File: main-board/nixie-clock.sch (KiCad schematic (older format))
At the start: 9 parts

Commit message: Rozdzielenie projektu
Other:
- note added: "Zamienić na EXTI?"
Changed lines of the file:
@@
 Text Label 9500 3850 2    60   ~ 0
 BRIGHT_POT
+Text Notes 9600 3850 0    60   ~ 0
+Zamienić na EXTI?
 $EndSCHEMATC

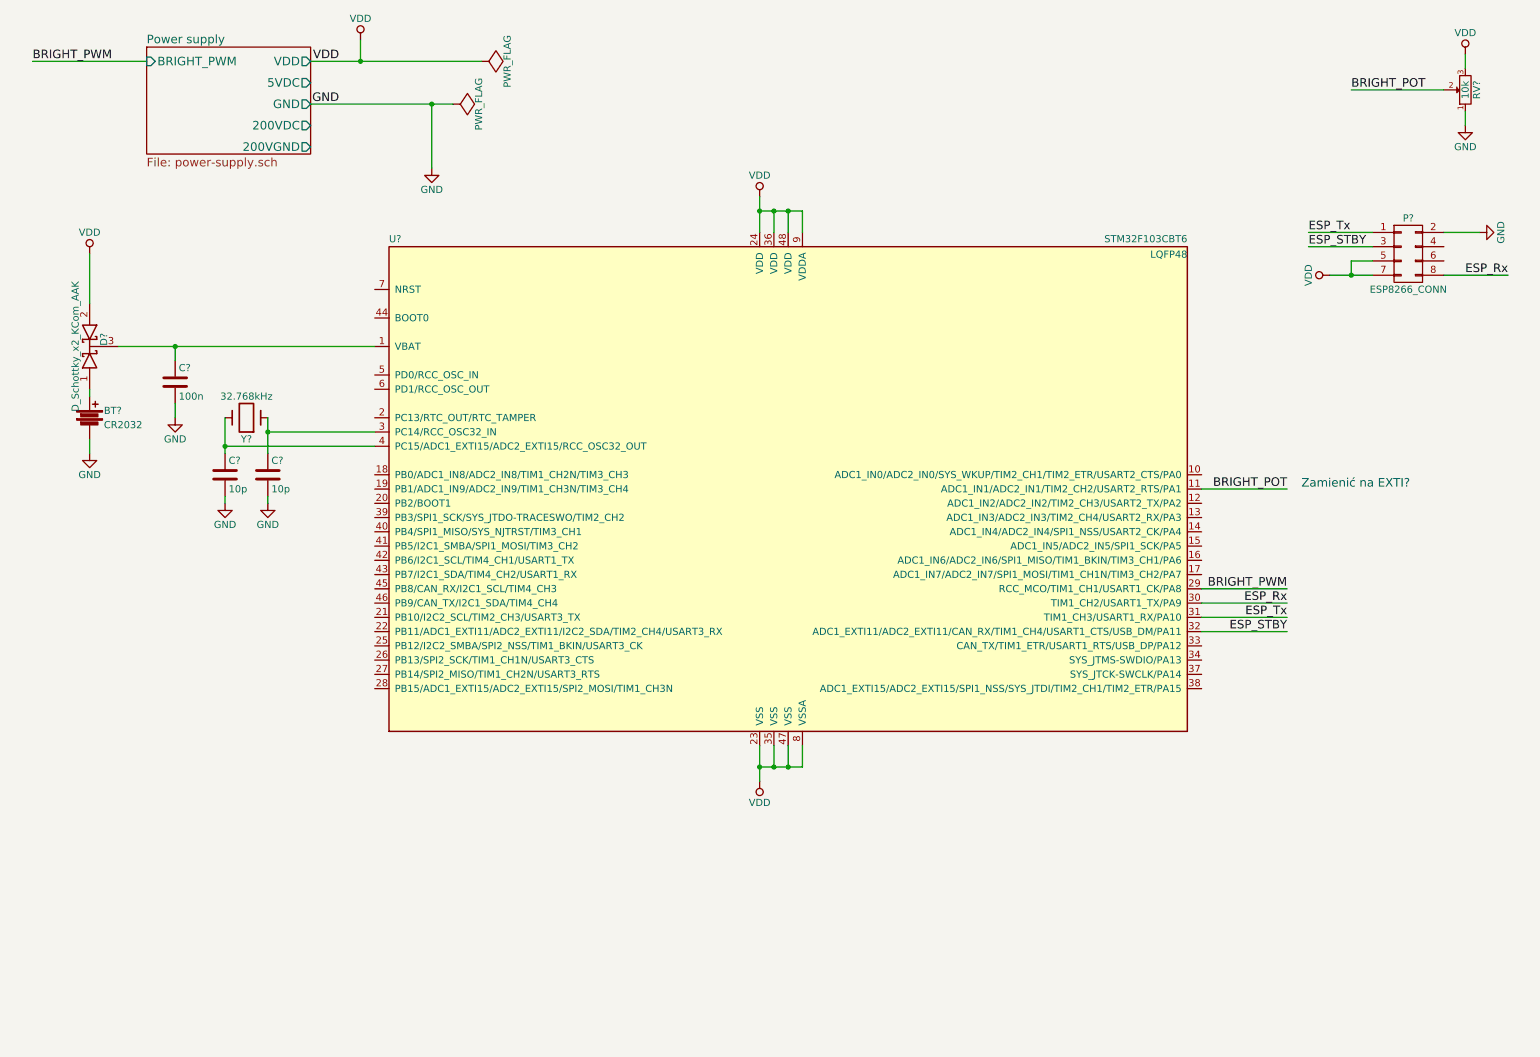
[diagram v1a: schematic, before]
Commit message: GPIO Expander - podlaczenie do STM32; wyprowadzenia dla modulow NIXIE; zasilanie - do poprawki (GPIO Expander zasilany z 5V - STM 3,3V
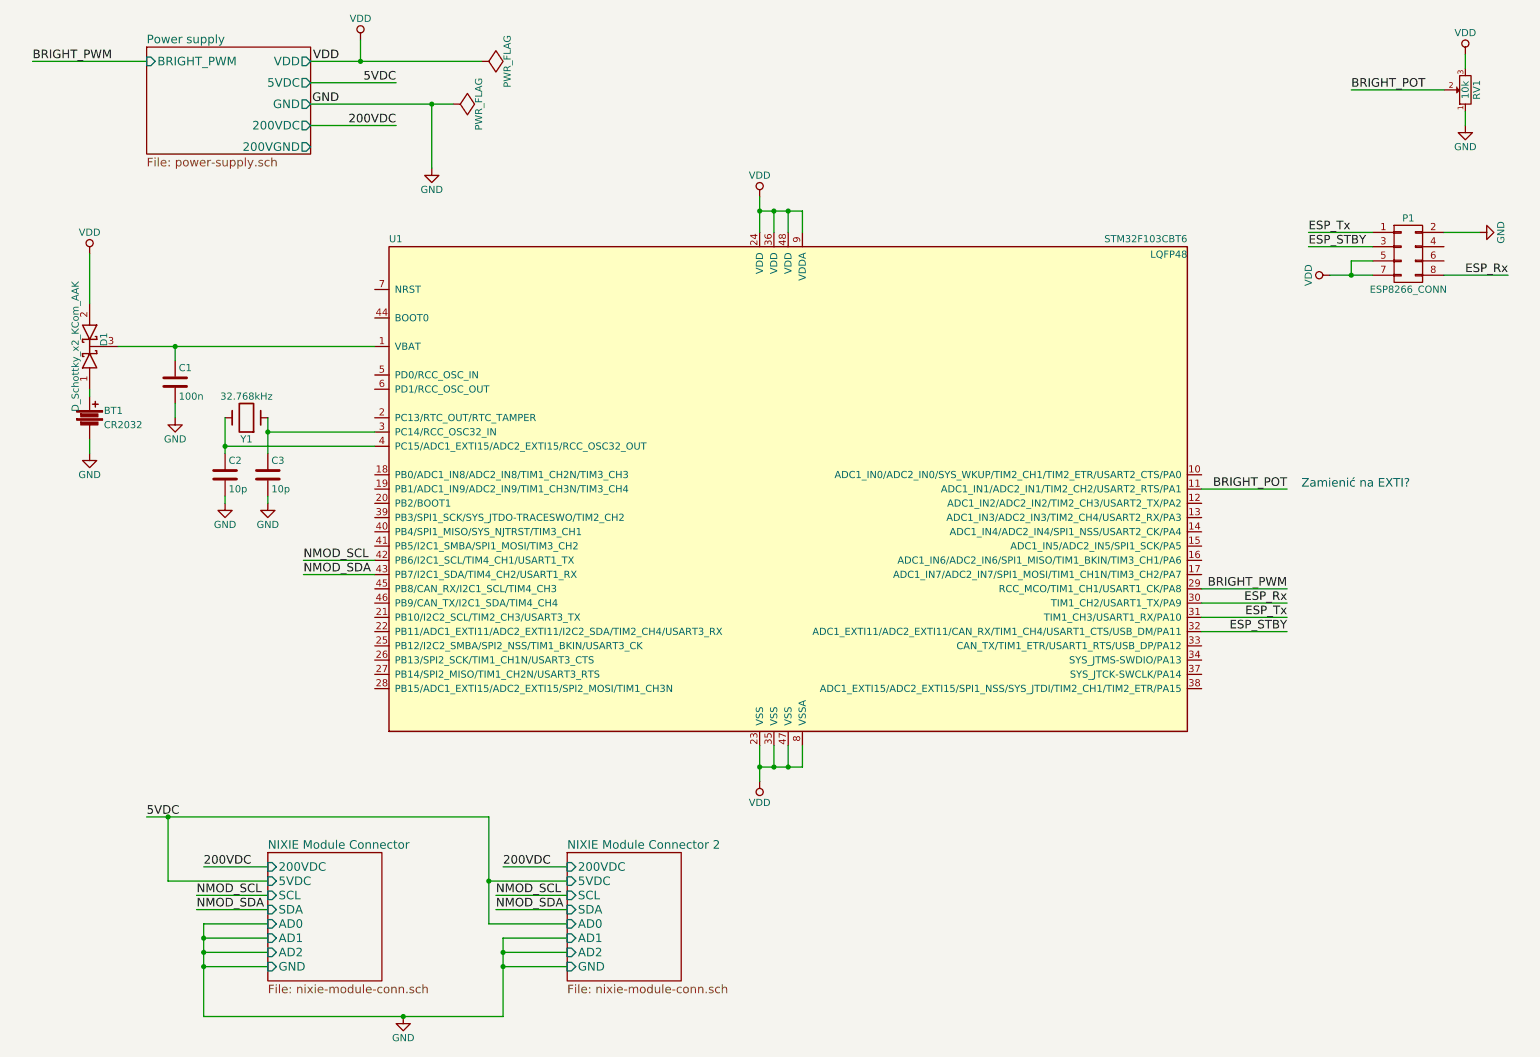
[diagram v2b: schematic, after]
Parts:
- gave numbers to parts that had none: 9
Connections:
- net NMOD_SCL: now reaches U1.42 (PB6/I2C1_SCL/TIM4_CH1/USART1_TX)
- net NMOD_SDA: now reaches U1.43 (PB7/I2C1_SDA/TIM4_CH2/USART1_RX)
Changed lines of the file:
@@
 $Descr A4 11693 8268
 encoding utf-8
-Sheet 1 2
+Sheet 1 4
 Title ""
 Date ""
@@
 $EndDescr
 $Comp
-L STM32F103CBTx U?
+L STM32F103CBTx U1
 U 1 1 5809D886
 P 6000 3850
-F 0 "U?" H 3200 5575 50  0000 L BNN
+F 0 "U1" H 3200 5575 50  0000 L BNN
 F 1 "STM32F103CBT6" H 8800 5575 50  0000 R BNN
 F 2 "LQFP48" H 8800 5525 50  0000 R TNN
@@
 $EndComp
 $Comp
-L Crystal Y?
+L Crystal Y1
 U 1 1 5809F07A
 P 2200 3350
-F 0 "Y?" H 2200 3500 50  0000 C CNN
+F 0 "Y1" H 2200 3500 50  0000 C CNN
 F 1 "32.768kHz" H 2200 3200 50  0000 C CNN
 F 2 "" H 2200 3350 50  0000 C CNN
@@
 	2050 3550 3100 3550
 $Comp
-L C C?
+L C C2
 U 1 1 5809F25A
 P 2050 3750
-F 0 "C?" H 2075 3850 50  0000 L CNN
+F 0 "C2" H 2075 3850 50  0000 L CNN
 F 1 "10p" H 2075 3650 50  0000 L CNN
 F 2 "" H 2088 3600 50  0000 C CNN
@@
 $EndComp
 $Comp
-L C C?
+L C C3
 U 1 1 5809F3ED
 P 2350 3750
-F 0 "C?" H 2375 3850 50  0000 L CNN
+F 0 "C3" H 2375 3850 50  0000 L CNN
 F 1 "10p" H 2375 3650 50  0000 L CNN
 F 2 "" H 2388 3600 50  0000 C CNN
@@
 $EndComp
 $Comp
-L GND #PWR?
+L GND #PWR01
 U 1 1 5809F415
 P 2050 3950
-F 0 "#PWR?" H 2050 3700 50  0001 C CNN
+F 0 "#PWR01" H 2050 3700 50  0001 C CNN
 F 1 "GND" H 2050 3800 50  0000 C CNN
 F 2 "" H 2050 3950 50  0000 C CNN
@@
 $EndComp
 $Comp
-L GND #PWR?
+L GND #PWR02
 U 1 1 5809F43C
 P 2350 3950
-F 0 "#PWR?" H 2350 3700 50  0001 C CNN
+F 0 "#PWR02" H 2350 3700 50  0001 C CNN
 F 1 "GND" H 2350 3800 50  0000 C CNN
 F 2 "" H 2350 3950 50  0000 C CNN
@@
 	2350 3900 2350 3950
 $Comp
-L D_Schottky_x2_KCom_AAK D?
+L D_Schottky_x2_KCom_AAK D1
 U 1 1 580A07B6
 P 1100 2850
-F 0 "D?" H 1150 2750 50  0000 C CNN
+F 0 "D1" H 1150 2750 50  0000 C CNN
 F 1 "D_Schottky_x2_KCom_AAK" H 1100 2950 50  0000 C CNN
 F 2 "" H 1100 2850 50  0000 C CNN
@@
 Connection ~ 1700 2850
 $Comp
-L C C?
+L C C1
 U 1 1 580A0B7E
 P 1700 3100
-F 0 "C?" H 1725 3200 50  0000 L CNN
+F 0 "C1" H 1725 3200 50  0000 L CNN
 F 1 "100n" H 1725 3000 50  0000 L CNN
 F 2 "" H 1738 2950 50  0000 C CNN
@@
 $EndComp
 $Comp
-L GND #PWR?
+L GND #PWR03
 U 1 1 580A0C6B
 P 1700 3350
-F 0 "#PWR?" H 1700 3100 50  0001 C CNN
+F 0 "#PWR03" H 1700 3100 50  0001 C CNN
 F 1 "GND" H 1700 3200 50  0000 C CNN
 F 2 "" H 1700 3350 50  0000 C CNN
@@
 	1700 3350 1700 3250
 $Comp
-L Battery BT?
+L Battery BT1
 U 1 1 580A0D26
 P 1100 3350
-F 0 "BT?" H 1200 3400 50  0000 L CNN
+F 0 "BT1" H 1200 3400 50  0000 L CNN
 F 1 "CR2032" H 1200 3300 50  0000 L CNN
 F 2 "" V 1100 3390 50  0000 C CNN
@@
 	1100 3200 1100 3150
 $Comp
-L GND #PWR?
+L GND #PWR04
 U 1 1 580A0DB8
 P 1100 3600
-F 0 "#PWR?" H 1100 3350 50  0001 C CNN
+F 0 "#PWR04" H 1100 3350 50  0001 C CNN
 F 1 "GND" H 1100 3450 50  0000 C CNN
 F 2 "" H 1100 3600 50  0000 C CNN
@@
 $EndSheet
 $Comp
-L PWR_FLAG #FLG?
+L PWR_FLAG #FLG05
 U 1 1 581749DC
 P 3850 850
-F 0 "#FLG?" H 3850 945 50  0001 C CNN
+F 0 "#FLG05" H 3850 945 50  0001 C CNN
 F 1 "PWR_FLAG" H 3850 1030 50  0000 C CNN
 F 2 "" H 3850 850 50  0000 C CNN
@@
 $EndComp
 $Comp
-L PWR_FLAG #FLG?
+L PWR_FLAG #FLG06
 U 1 1 58174A1B
 P 3650 1150
-F 0 "#FLG?" H 3650 1245 50  0001 C CNN
+F 0 "#FLG06" H 3650 1245 50  0001 C CNN
 F 1 "PWR_FLAG" H 3650 1330 50  0000 C CNN
 F 2 "" H 3650 1150 50  0000 C CNN
@@
 Connection ~ 6000 5800
 $Comp
-L GND #PWR?
+L GND #PWR07
 U 1 1 58173306
 P 3500 1600
-F 0 "#PWR?" H 3500 1350 50  0001 C CNN
+F 0 "#PWR07" H 3500 1350 50  0001 C CNN
 F 1 "GND" H 3500 1450 50  0000 C CNN
 F 2 "" H 3500 1600 50  0000 C CNN
@@
 Connection ~ 3500 1150
 $Comp
-L VDD #PWR?
+L VDD #PWR08
 U 1 1 58175A0D
 P 3000 700
-F 0 "#PWR?" H 3000 550 50  0001 C CNN
+F 0 "#PWR08" H 3000 550 50  0001 C CNN
 F 1 "VDD" H 3000 850 50  0000 C CNN
 F 2 "" H 3000 700 50  0000 C CNN
@@
 $EndComp
 $Comp
-L VDD #PWR?
+L VDD #PWR09
 U 1 1 58176266
 P 1100 2200
-F 0 "#PWR?" H 1100 2050 50  0001 C CNN
+F 0 "#PWR09" H 1100 2050 50  0001 C CNN
 F 1 "VDD" H 1100 2350 50  0000 C CNN
 F 2 "" H 1100 2200 50  0000 C CNN
@@
 $EndComp
 $Comp
-L VDD #PWR?
+L VDD #PWR010
 U 1 1 58176451
 P 5800 1800
-F 0 "#PWR?" H 5800 1650 50  0001 C CNN
+F 0 "#PWR010" H 5800 1650 50  0001 C CNN
 F 1 "VDD" H 5800 1950 50  0000 C CNN
 F 2 "" H 5800 1800 50  0000 C CNN
@@
 $EndComp
 $Comp
-L VDD #PWR?
+L VDD #PWR011
 U 1 1 58176B17
 P 5800 5900
-F 0 "#PWR?" H 5800 5750 50  0001 C CNN
+F 0 "#PWR011" H 5800 5750 50  0001 C CNN
 F 1 "VDD" H 5800 6050 50  0000 C CNN
 F 2 "" H 5800 5900 50  0000 C CNN
@@
 Connection ~ 3000 850
 $Comp
-L CONN_02X04 P?
+L CONN_02X04 P1
 U 1 1 5817ACF2
 P 10350 2200
-F 0 "P?" H 10350 2450 50  0000 C CNN
+F 0 "P1" H 10350 2450 50  0000 C CNN
 F 1 "ESP8266_CONN" H 10350 1950 50  0000 C CNN
 F 2 "" H 10350 1000 50  0000 C CNN
@@
 	10600 2050 10850 2050
 $Comp
-L GND #PWR?
+L GND #PWR012
 U 1 1 5817B257
 P 10850 2050
-F 0 "#PWR?" H 10850 1800 50  0001 C CNN
+F 0 "#PWR012" H 10850 1800 50  0001 C CNN
 F 1 "GND" H 10850 1900 50  0000 C CNN
 F 2 "" H 10850 2050 50  0000 C CNN
@@
 $EndComp
 $Comp
-L VDD #PWR?
+L VDD #PWR013
 U 1 1 5817B5C8
 P 9800 2350
-F 0 "#PWR?" H 9800 2200 50  0001 C CNN
+F 0 "#PWR013" H 9800 2200 50  0001 C CNN
 F 1 "VDD" H 9800 2500 50  0000 C CNN
 F 2 "" H 9800 2350 50  0000 C CNN
@@
 BRIGHT_PWM
 $Comp
-L POT RV?
+L POT RV1
 U 1 1 58181F47
 P 10750 1050
-F 0 "RV?" H 10750 970 50  0000 C CNN
+F 0 "RV1" H 10750 970 50  0000 C CNN
 F 1 "10k" H 10750 1050 50  0000 C CNN
 F 2 "" H 10750 1050 50  0000 C CNN
@@
 	10750 1200 10750 1300
 $Comp
-L VDD #PWR?
+L VDD #PWR014
 U 1 1 58182C82
 P 10750 800
-F 0 "#PWR?" H 10750 650 50  0001 C CNN
+F 0 "#PWR014" H 10750 650 50  0001 C CNN
 F 1 "VDD" H 10750 950 50  0000 C CNN
 F 2 "" H 10750 800 50  0000 C CNN
@@
 $EndComp
 $Comp
-L GND #PWR?
+L GND #PWR015
 U 1 1 58182F5B
 P 10750 1300
-F 0 "#PWR?" H 10750 1050 50  0001 C CNN
+F 0 "#PWR015" H 10750 1050 50  0001 C CNN
 F 1 "GND" H 10750 1150 50  0000 C CNN
 F 2 "" H 10750 1300 50  0000 C CNN
@@
 Text Notes 9600 3850 0    60   ~ 0
 Zamienić na EXTI?
+$Sheet
+S 2350 6400 800  900
+U 58191DB1
+F0 "NIXIE Module Connector" 60
+F1 "nixie-module-conn.sch" 60
+F2 "SCL" I L 2350 6700 60
+F3 "SDA" I L 2350 6800 60
+F4 "AD0" I L 2350 6900 60
+F5 "AD1" I L 2350 7000 60
+F6 "AD2" I L 2350 7100 60
+F7 "5VDC" I L 2350 6600 60
+F8 "GND" I L 2350 7200 60
+F9 "200VDC" I L 2350 6500 60
+$EndSheet
+$Sheet
+S 4450 6400 800  900
+U 581979CF
+F0 "NIXIE Module Connector 2" 60
+F1 "nixie-module-conn.sch" 60
+F2 "SCL" I L 4450 6700 60
+F3 "SDA" I L 4450 6800 60
+F4 "AD0" I L 4450 6900 60
+F5 "AD1" I L 4450 7000 60
+F6 "AD2" I L 4450 7100 60
+F7 "5VDC" I L 4450 6600 60
+F8 "GND" I L 4450 7200 60
+F9 "200VDC" I L 4450 6500 60
+$EndSheet
+Wire Wire Line
+	2650 1300 3250 1300
+Wire Wire Line
+	2650 1000 3250 1000
+Text Label 3250 1000 2    60   ~ 0
+5VDC
+Text Label 3250 1300 2    60   ~ 0
+200VDC
+Wire Wire Line
+	2350 6500 1900 6500
+Text Label 1900 6500 0    60   ~ 0
+200VDC
+Wire Wire Line
+	1650 6600 2350 6600
+Text Label 4000 6500 0    60   ~ 0
+200VDC
+Text Label 1500 6150 0    60   ~ 0
+5VDC
+Wire Wire Line
+	4000 6500 4450 6500
+Wire Wire Line
+	3900 6600 4450 6600
+$Comp
+L GND #PWR?
+U 1 1 5819F48F
+P 3300 7550
+F 0 "#PWR?" H 3300 7300 50  0001 C CNN
+F 1 "GND" H 3300 7400 50  0000 C CNN
+F 2 "" H 3300 7550 50  0000 C CNN
+F 3 "" H 3300 7550 50  0000 C CNN
+	1    3300 7550
+	1    0    0    -1
+$EndComp
+Wire Wire Line
+	4450 7200 4000 7200
+Wire Wire Line
+	4000 7000 4000 7550
+Wire Wire Line
+	4000 7550 1900 7550
+Wire Wire Line
+	1900 7550 1900 6900
+Wire Wire Line
+	1900 7200 2350 7200
+Connection ~ 3300 7550
+Wire Wire Line
+	1650 6150 1650 6600
+Wire Wire Line
+	1500 6150 3900 6150
+Wire Wire Line
+	3900 6150 3900 6900
+Connection ~ 1650 6150
+Wire Wire Line
+	1900 6900 2350 6900
+Connection ~ 1900 7200
+Wire Wire Line
+	2350 7000 1900 7000
+Connection ~ 1900 7000
+Wire Wire Line
+	2350 7100 1900 7100
+Connection ~ 1900 7100
+Wire Wire Line
+	3900 6900 4450 6900
+Connection ~ 3900 6600
+Wire Wire Line
+	4450 7000 4000 7000
+Connection ~ 4000 7200
+Wire Wire Line
+	4450 7100 4000 7100
+Connection ~ 4000 7100
+Wire Wire Line
+	2600 4350 3100 4350
+Wire Wire Line
+	2600 4450 3100 4450
+Text Label 2600 4350 0    60   ~ 0
+NMOD_SCL
+Text Label 2600 4450 0    60   ~ 0
+NMOD_SDA
+Wire Wire Line
+	1850 6700 2350 6700
+Wire Wire Line
+	1850 6800 2350 6800
+Wire Wire Line
+	3950 6700 4450 6700
+Wire Wire Line
+	3950 6800 4450 6800
+Text Label 3950 6700 0    60   ~ 0
+NMOD_SCL
+Text Label 3950 6800 0    60   ~ 0
+NMOD_SDA
+Text Label 1850 6700 0    60   ~ 0
+NMOD_SCL
+Text Label 1850 6800 0    60   ~ 0
+NMOD_SDA
 $EndSCHEMATC

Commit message: Dokumentacja STM32F103CBT6; poprawki zasilania, podciagniecie linii SDA i SCL, kondensator przy ESP8266 #1
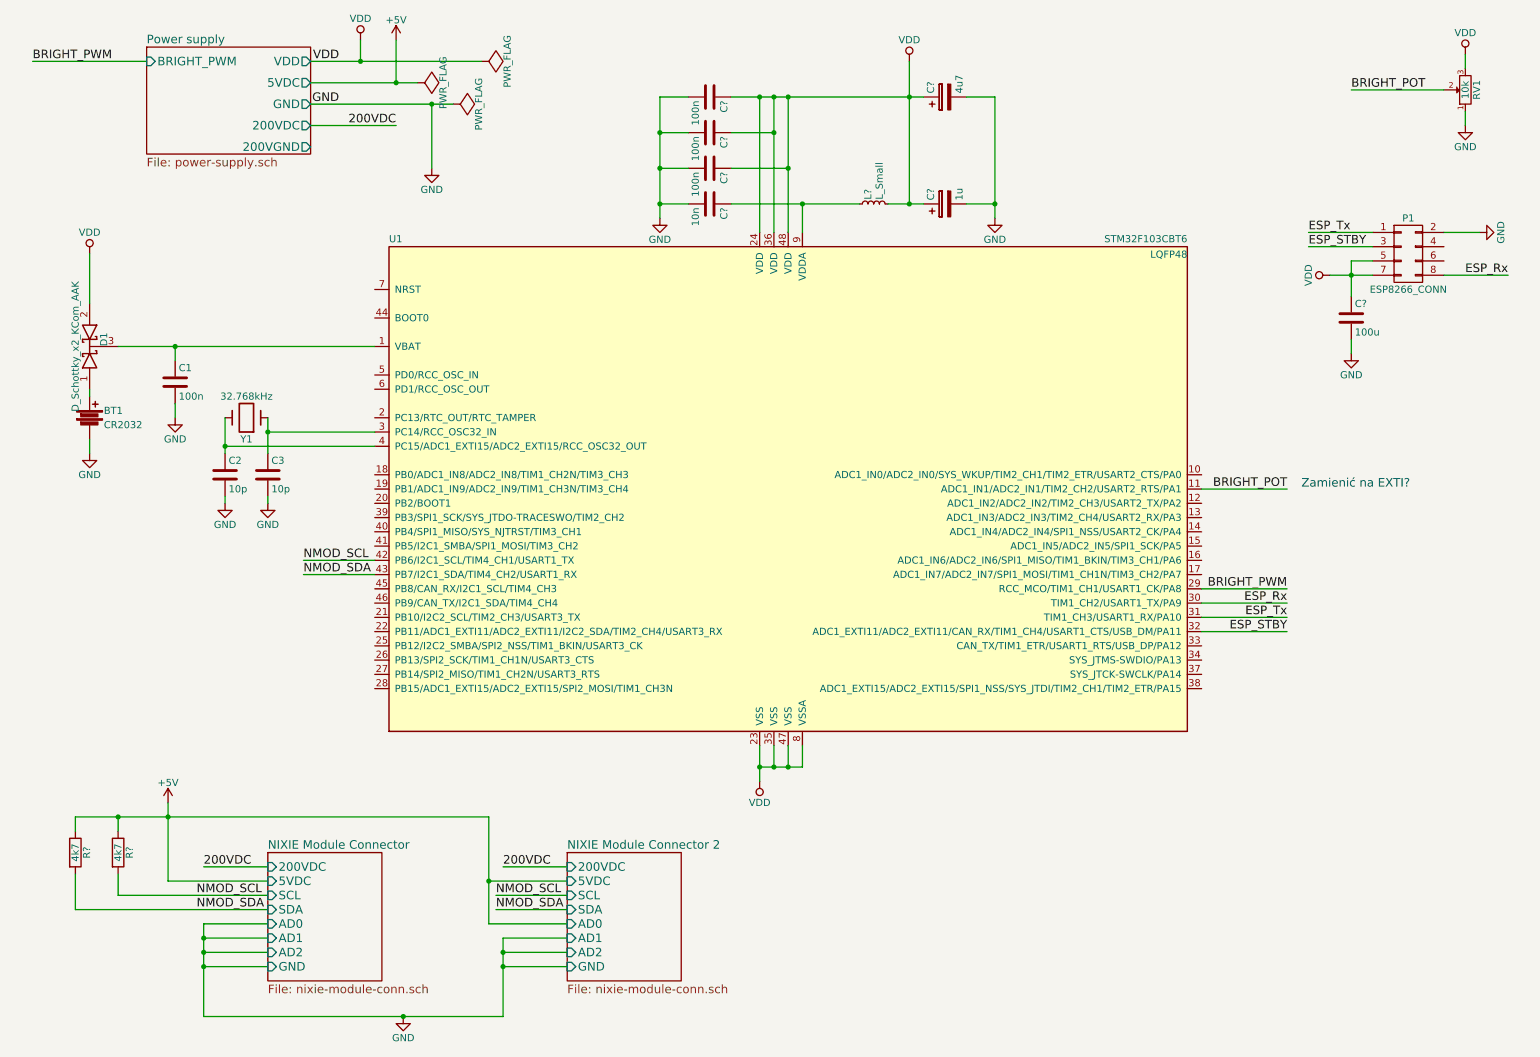
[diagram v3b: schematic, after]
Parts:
- added C?: 100u, symbol C
- added C? (x3): 100n, symbol C
- added C?: 10n, symbol C
- added C?: 4u7, symbol CP
- added C?: 1u, symbol CP
- added L?: L_Small, symbol L_Small
- added R? (x2): 4k7, symbol R
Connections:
- net GND: now also C?.2, C?.2, C?.2, C?.2, C?.2, C?.2, C?.2
- net NMOD_SCL: now also R?.2
- net NMOD_SDA: now also R?.2
- net VDD: now also C?.1, C?.1, C?.1, C?.1, C?.1, C?.1, L?.2; no longer U1.9 (VDDA)
- new net: C?.1, L?.1, U1.9 (VDDA)
- new net +5V: R?.1, R?.1
